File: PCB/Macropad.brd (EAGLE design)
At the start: 133.3 x 145 mm, 84 parts, among them IC1 LM2937, J1 54819-0519

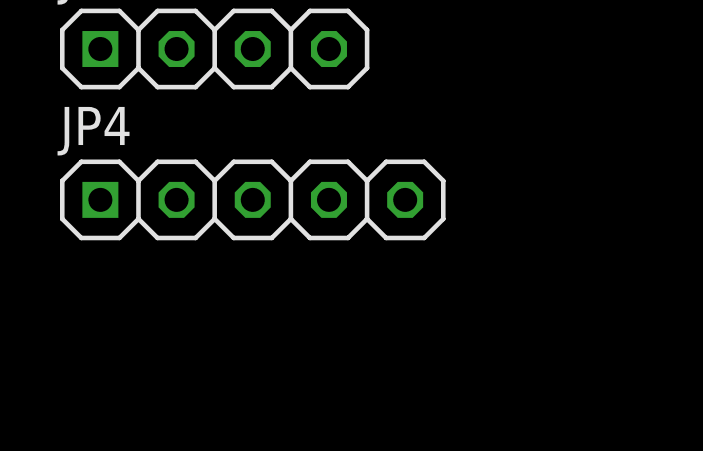
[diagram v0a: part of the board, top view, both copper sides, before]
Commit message: Added JTAG connection
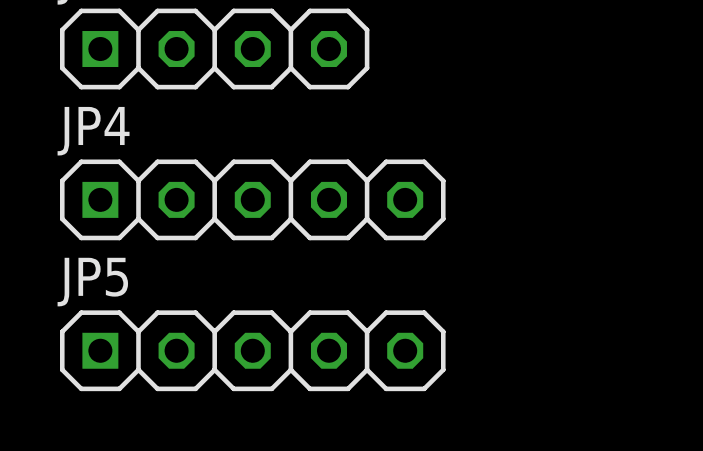
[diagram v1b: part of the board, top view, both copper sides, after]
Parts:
- added JP5: (no value), EE445L:1X05
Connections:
- new net TCK: JP5.5, U$1.52
- new net TDI: JP5.3, U$1.50
- new net TDO: JP5.2, U$1.49
- new net TMS: JP5.4, U$1.51
- net GND: now also JP5.1
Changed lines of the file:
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@@
 <attribute name="VALUE" x="-78.5368" y="-385.5974" size="1.27" layer="27"/>
+</element>
+<element name="JP5" library="EE445L" package="1X05" value="" x="-72.1868" y="-387.4516" smashed="yes">
+<attribute name="NAME" x="-78.613" y="-385.6228" size="1.27" layer="25" ratio="10"/>
+<attribute name="VALUE" x="-78.5368" y="-390.6266" size="1.27" layer="27"/>
 </element>
 </elements>
@@
 <contactref element="J1" pad="10"/>
 <contactref element="J1" pad="5"/>
+<contactref element="JP5" pad="1"/>
+<wire x1="-72.3904" y1="-355.854" x2="-77.2668" y2="-387.4516" width="0" layer="19" extent="1-1"/>
 <wire x1="-72.3904" y1="-355.579" x2="-72.3904" y2="-355.854" width="0" layer="19" extent="16-16"/>
 <wire x1="71.8566" y1="23.7744" x2="-72.3904" y2="-355.579" width="0" layer="19" extent="1-16"/>
@@
 <wire x1="63.2436" y1="81.2012" x2="-67.1068" y2="-382.4224" width="0" layer="19" extent="1-1"/>
 </signal>
+<signal name="TDO">
+<contactref element="U$1" pad="49"/>
+<contactref element="JP5" pad="2"/>
+<wire x1="51.7676" y1="83.2012" x2="-74.7268" y2="-387.4516" width="0" layer="19" extent="1-1"/>
+</signal>
+<signal name="TDI">
+<contactref element="U$1" pad="50"/>
+<contactref element="JP5" pad="3"/>
+<wire x1="51.7676" y1="82.7012" x2="-72.1868" y2="-387.4516" width="0" layer="19" extent="1-1"/>
+</signal>
+<signal name="TMS">
+<contactref element="U$1" pad="51"/>
+<contactref element="JP5" pad="4"/>
+<wire x1="51.7676" y1="82.2012" x2="-69.6468" y2="-387.4516" width="0" layer="19" extent="1-1"/>
+</signal>
+<signal name="TCK">
+<contactref element="U$1" pad="52"/>
+<contactref element="JP5" pad="5"/>
+<wire x1="51.7676" y1="81.7012" x2="-67.1068" y2="-387.4516" width="0" layer="19" extent="1-1"/>
+</signal>
 </signals>

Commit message: Started pcb layout
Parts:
- removed 3.3V, 5.0V, GND, GND1: TP_LOOP, EE445L:TP_LOOP
- moved J1 516.2 mm to (108.3, 126.5), turned to 180 degrees
- moved JP4 432.9 mm to (118.2, 6.35)
- moved JP3 423.4 mm to (105.5, 6.35)
- moved JP5 422.5 mm to (90.4, 2.54)
- moved JP1 412.1 mm to (91.6, 6.35)
- moved S21 358.5 mm to (12.7, 12.7)
- moved S5 292.8 mm to (12.7, 99.1)
- moved D1 277.9 mm to (2.29, 118.1), turned to 90 degrees
- moved S4 169.9 mm to (73.7, 120.7)
- moved S3 144.2 mm to (53.3, 120.7)
- moved S2 123.8 mm to (33.0, 120.7)
- moved S1 111.9 mm to (12.7, 120.7)
- moved R2 71.2 mm to (114.2, 45.8)
- moved C1 69.6 mm to (105.7, 14.5)
- moved C10 69.6 mm to (114.1, 25.2)
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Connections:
- net N$1 renamed OSC1
- net N$2 renamed OSC0
- net N$5 renamed +5V_POWER
- net N$7 renamed LED_IN
- net N$8 renamed RESET
- net N$9 renamed WAKE
- net +3V3: no longer 3.3V.P$1, 3.3V.P$2
- net +5V: no longer 5.0V.P$1, 5.0V.P$2
- net GND: no longer GND.P$1, GND.P$2, GND1.P$1, GND1.P$2
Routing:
- net +3V3: track 278.6 -> 47.3 mm
- net GND: track 261.4 -> 106.1 mm
- net +5V: track 95.2 -> 0.00 mm
- net WAKE: track 53.5 -> 0.10 mm
- net ST7735_RST: track 52.2 -> 0.00 mm, vias 2 -> 0
- net ST7735_DC: track 48.4 -> 0.00 mm, vias 2 -> 0
- net RESET: track 43.1 -> 1.03 mm
- net ST7735_MOSI: track 38.7 -> 0.00 mm, vias 2 -> 0
- net ST7735_TFT_CS: track 38.3 -> 0.00 mm, vias 2 -> 0
- net ST7735_SCK: track 33.2 -> 0.00 mm, vias 2 -> 0
- net ST7735_MISO: track 32.1 -> 0.00 mm, vias 2 -> 0
- net +5V_POWER: track 6.52 -> 0.00 mm
- net LED_IN: track 4.78 -> 0.00 mm
- net VDDC: track 25.4 -> 22.0 mm
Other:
- board size 133.3 x 145 mm -> 127 x 133.3 mm
- board text removed: "EE445L Lab 6 - Fall 2021 William Avery TA: Matthew Yu Audio Device"

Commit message: Added rotary encoder
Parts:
- added U1: EC11E09244AQ, SamacSys_Parts:EC11E09244AQ
- moved D13 299.9 mm to (-85.3, -54.1)
- moved D14 299.9 mm to (-70.9, -54.1)
- moved D15 299.9 mm to (-56.5, -54.1)
- moved D16 299.9 mm to (-42.2, -54.1)
- moved D17 299.9 mm to (-27.8, -54.1)
- moved D2 299.9 mm to (-85.3, 139.7)
- moved D3 299.9 mm to (-85.3, 133.4)
- moved D4 299.9 mm to (-85.3, 127.1)
- moved D5 299.9 mm to (-85.3, 78.0)
- moved D6 299.9 mm to (-70.9, 78.0)
- moved D7 299.9 mm to (-85.3, 71.7)
- moved D8 299.9 mm to (-70.9, 71.7)
- moved S10 299.9 mm to (-65.7, 57.8)
- moved S11 299.9 mm to (-81.7, 36.4)
- moved S12 299.9 mm to (-65.7, 36.4)
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- renumbered JP5 to JTAG
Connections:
- net GND: now also J1.11, J1.12, J1.S1, J1.S2, U1.C1, U1.E1
- net PF0: now also U1.A1
- net PF1: now also U1.B1
- net PF2: now also U1.D1

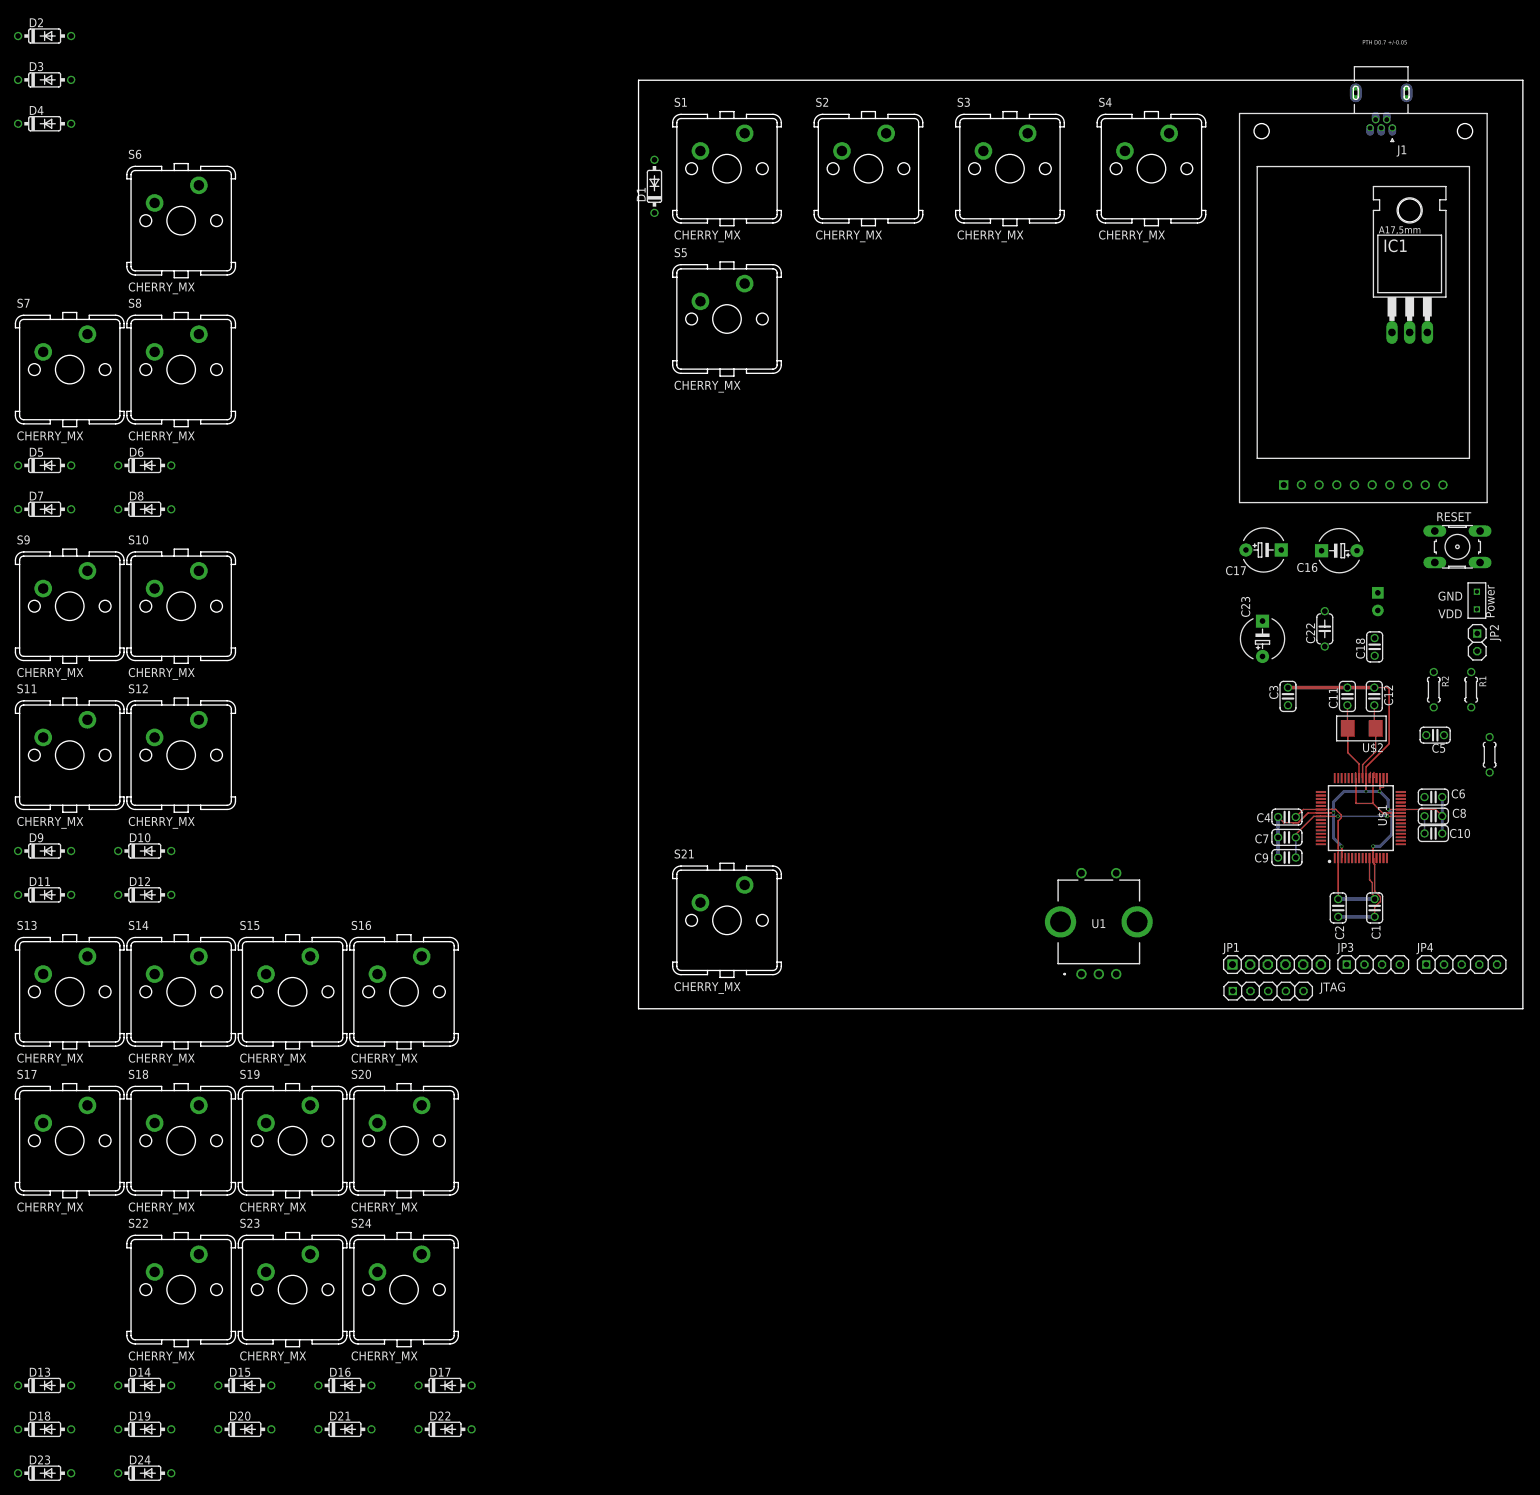
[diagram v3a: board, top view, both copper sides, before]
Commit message: Finished first draft of PCB layout
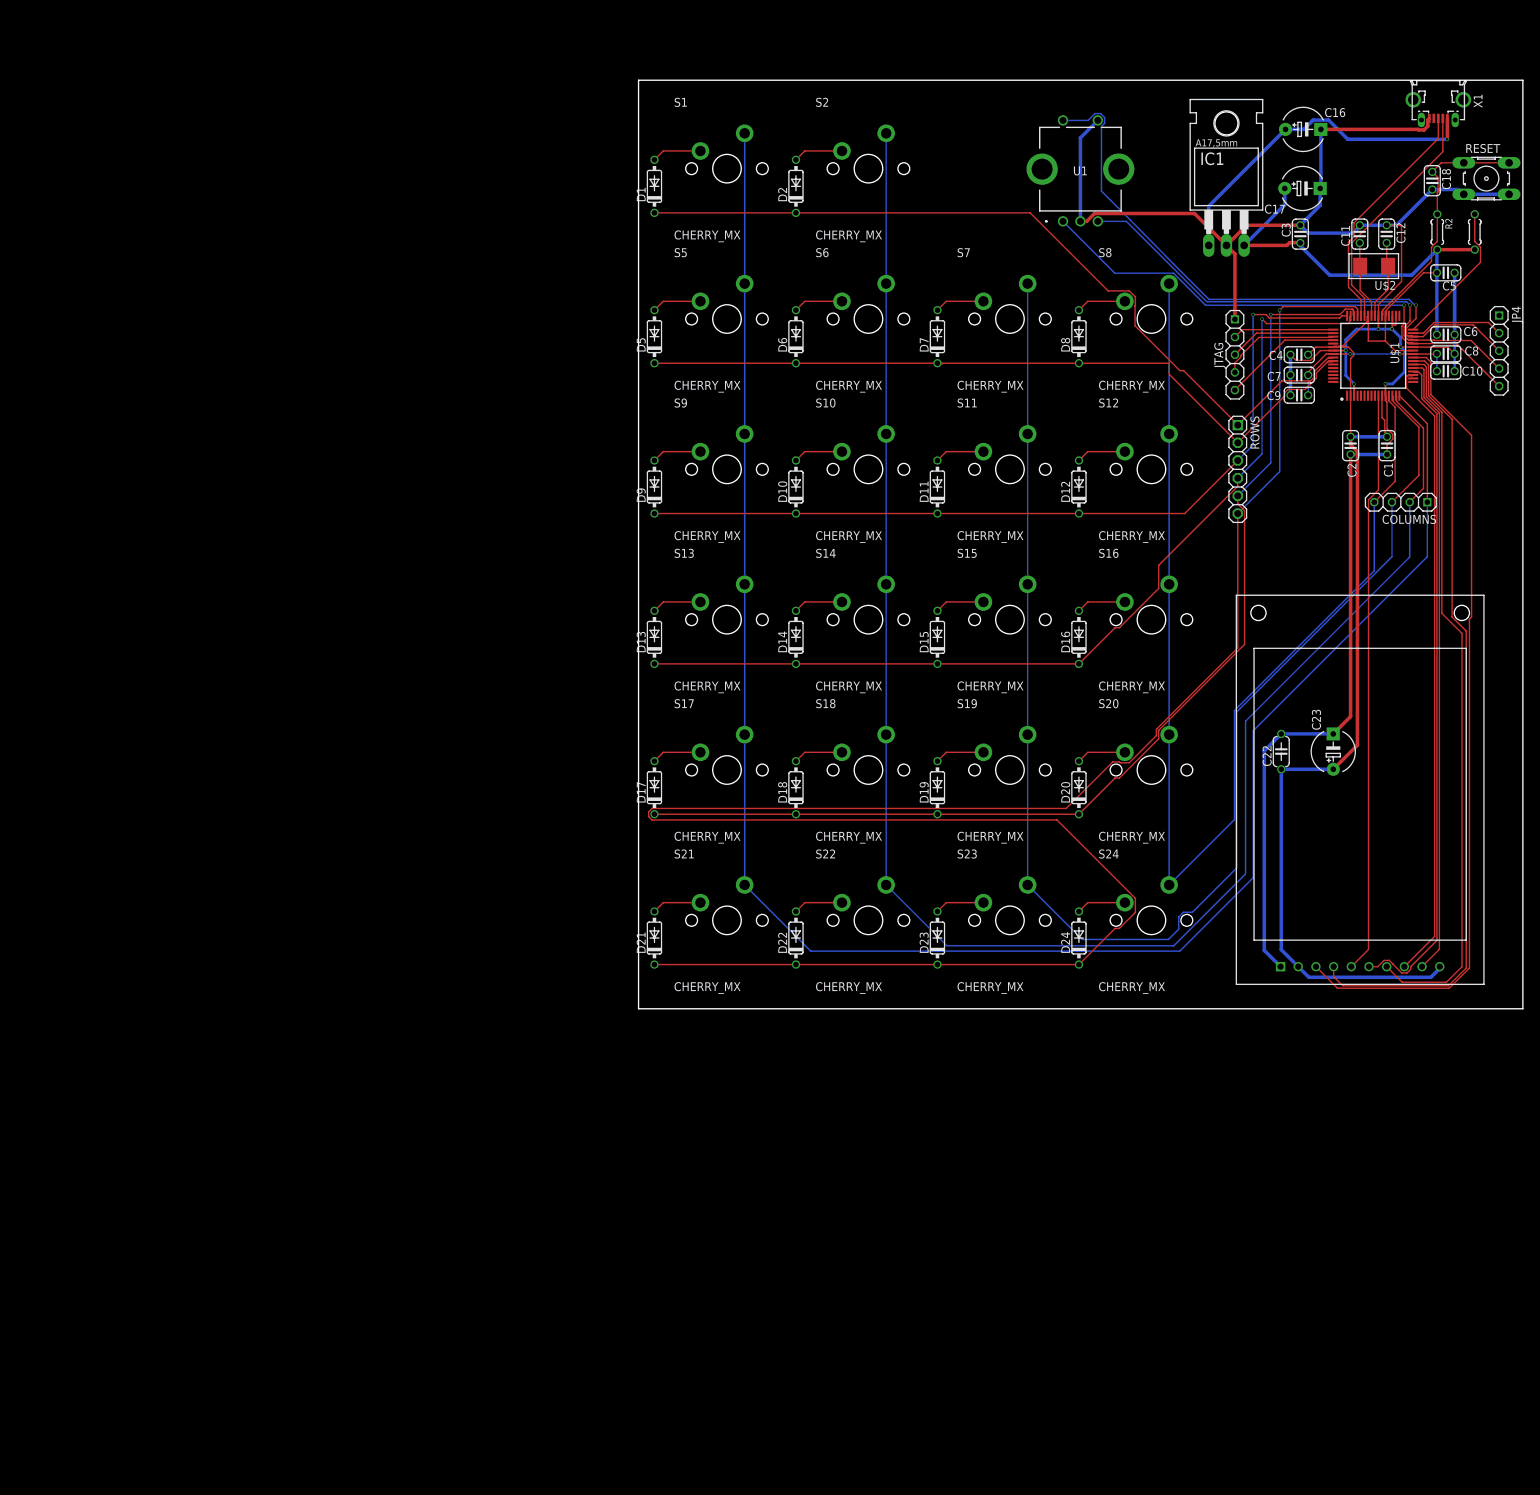
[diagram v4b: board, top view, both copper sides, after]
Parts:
- removed D3, D4: 1N914DO35-7, EE445L:DO35-7
- removed J1: 54819-0519, 54819-0519:MOLEX_54819-0519
- removed JP1: (no value), EE445L:1X06
- removed JP2: (no value), EE445L:1X02
- removed JP3: (no value), EE445L:1X04
- removed LED2: (no value), EE445L:LED3MM
- removed R1: 1K, EE445L:RES200MIL
- removed S3, S4: CHERRY_MX, cherry:CHERRY_MX
- removed U$4: POWER_CONN, EE445L:POWER_CONN
- added COLUMNS: (no value), EE445L:1X04
- added ROWS: (no value), EE445L:1X06
- added X1: ZX62D-B-5PA8, zx62d-b-5pa8-oshpark_10:ZX62D-B-5PA8
- moved D24 154.6 mm to (63.2, 10.2), turned to 90 degrees
- moved D20 151.1 mm to (63.2, 31.8), turned to 90 degrees
- moved D16 150.5 mm to (63.2, 53.3), turned to 90 degrees
- moved D23 149.5 mm to (42.9, 10.2), turned to 90 degrees
- moved D19 146.5 mm to (42.9, 31.8), turned to 90 degrees
- moved D15 146.4 mm to (42.9, 53.3), turned to 90 degrees
- moved D12 146.4 mm to (63.2, 74.9), turned to 90 degrees
- moved S12 145.3 mm to (73.7, 77.5)
- moved D14 142.4 mm to (22.6, 53.3), turned to 90 degrees
- moved D18 141.9 mm to (22.6, 31.8), turned to 90 degrees
- moved S11 141.1 mm to (53.3, 77.5)
- moved D11 141.0 mm to (42.9, 74.9), turned to 90 degrees
- moved S8 139.5 mm to (73.7, 99.1)
- moved D13 138.6 mm to (2.29, 53.3), turned to 90 degrees
- moved D8 136.4 mm to (63.2, 96.5), turned to 90 degrees
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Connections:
- removed net +5V_POWER: JP2.1, U$4.VDD
- removed net COLUMN_4: JP1.5
- removed net COLUMN_5: JP1.6
- removed net LED_IN: LED2.A, R1.1
- removed net N$10: D4.A, S4.S1
- removed net N$6: D3.A, S3.S1
- removed net PF4: JP4.1, U$1.5
- net +3V3: no longer R1.2
- net +5V: now also X1.1; no longer J1.1, J1.6, JP2.2
- net COLUMN_0: now also COLUMNS.1; no longer JP1.1
- net COLUMN_1: now also COLUMNS.2; no longer JP1.2
- net COLUMN_2: now also COLUMNS.3; no longer JP1.3, S3.S2
- net COLUMN_3: now also COLUMNS.4; no longer JP1.4, S4.S2
- net D+: now also X1.3; no longer J1.3, J1.8
- net D-: now also X1.2; no longer J1.2, J1.7
- net GND: now also X1.5; no longer J1.10, J1.11, J1.12, J1.5, J1.S1, J1.S2, LED2.K, U$4.GND
- net ROW_0: now also ROWS.1; no longer D3.C, D4.C, JP3.1
- net ROW_1: now also ROWS.2; no longer JP3.2
- net ROW_2: now also ROWS.3; no longer JP3.3
- net ROW_3: now also ROWS.4; no longer JP3.4
- net ROW_4: now also ROWS.5
- net ROW_5: now also ROWS.6
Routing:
- net ROW_5: track 0.00 -> 308.1 mm, vias 0 -> 1
- net COLUMN_0: track 0.00 -> 270.5 mm
- net COLUMN_1: track 0.00 -> 248.4 mm
- net GND: track 106.1 -> 313.3 mm
- net COLUMN_2: track 0.00 -> 205.1 mm
- net +3V3: track 47.3 -> 230.9 mm
- net COLUMN_3: track 0.00 -> 170.4 mm
- net ROW_4: track 0.00 -> 158.4 mm, vias 0 -> 1
- net ROW_3: track 0.00 -> 135.6 mm, vias 0 -> 1
- net ROW_2: track 0.00 -> 122.6 mm, vias 0 -> 1
- net ROW_0: track 0.00 -> 117.2 mm
- net ST7735_RST: track 0.00 -> 116.9 mm
- net ST7735_DC: track 0.00 -> 113.4 mm
- net ROW_1: track 0.00 -> 110.1 mm
- net ST7735_MOSI: track 0.00 -> 103.0 mm
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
